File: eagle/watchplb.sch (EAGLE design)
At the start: 53 parts, among them IC1 SAM-M8Q, IC2 BM70BLES1FC2-0B03AA, Q1 8MHz / LFXTAL020423Reel, U1 MCP111-XXXXX/TO, U2 STM32L073RZ, U3 MCP2200-I/SS

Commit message: update
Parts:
- added C19: CSTCE12M0G15L99-R0, 12mhz osc:CSTCE8M00G52-R0
- added C20: 1uF, resistor:C-EUC0805
- added D1: S8NC-13, diode:DIODE-SMC
- added J1: (no value), SparkFun-Connectors:USB_MICRO-B_FEMALE-SMT
- added JP2: VIB_MOTOR, 619-28821, pinhead:PINHD-1X2
- added LED10: YELLOW, adafruit:LEDCHIP-LED0805
- added LED11, LED6, LED7, LED8: GREEN, adafruit:LEDCHIP-LED0805
- added LED12, LED9: RED, adafruit:LEDCHIP-LED0805
- added Q2: DMT5015LFDF, Hick:DMT5015LFDF
- added R18, R19, R20, R21, R22, R23, R24: 220R, resistor:R-EU_M0805
- added R25: 100k, resistor:R-EU_M0805
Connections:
- net N$10 renamed IND_LED_B
- net N$15 renamed IND_LED_W
- net N$17 renamed IND_LED_R
- net N$8 renamed IND_LED_G
- new net +5V: J1.VBUS, U3.VDD
- new net N$10: C19.33, U3.OSC2
- new net N$13: LED9.A, R21.2
- new net N$15: C19.11, U3.OSC1
- new net N$17: J1.D-, U3.D-
- new net N$19: LED6.A, R18.2
- new net N$20: J1.D+, U3.D+
- new net N$21: C20.1, U3.VUSB
- new net N$22: LED7.A, R19.2
- new net N$23: LED12.A, R24.2
- new net N$24: LED10.A, R22.2
- new net N$25: LED8.A, R20.2
- new net N$26: LED11.C, U3.GP6/RXLED
- new net N$27: LED12.C, U3.GP7/TXLED
- new net N$28: D1.A, JP2.2, Q2.D
- new net N$8: LED11.A, R23.2
- new net POW_LED_G1: R20.1, U2.PC4
- new net POW_LED_G2: R19.1, U2.PC5
- new net POW_LED_G3: R18.1, U2.PB0
- new net POW_LED_R: R21.1, U2.PA6
- new net POW_LED_Y: R22.1, U2.PA7
- new net SWD_RX: U3.RX
- new net SWD_RXD: U2.PA2
- new net SWD_TX: U3.TX
- new net SWD_TXD: U2.PA3
- new net V+: D1.C, JP2.1
- new net VIBRATOR: Q2.G, R25.1, U2.PA11
- net +3V3: now also R23.1, R24.1, U3.N_RST
- net GND: now also C19.22, C20.2, J1.GND, J1.SHIELD, LED10.C, LED6.C, LED7.C, LED8.C, LED9.C, Q2.S, R25.2, U3.VSS
- net GPS_RXD: now also U2.PC10; no longer U2.PA2
- net GPS_TXD: now also U2.PC11; no longer U2.PA3
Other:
- note added: "uart4 bzw lpuart1"
- note removed: "^^^^GPS UART2, crossed"
- moved on the sheet: C10, C11, C12, C13, C14, C15, C16, C17, C18, C4, C5, C6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

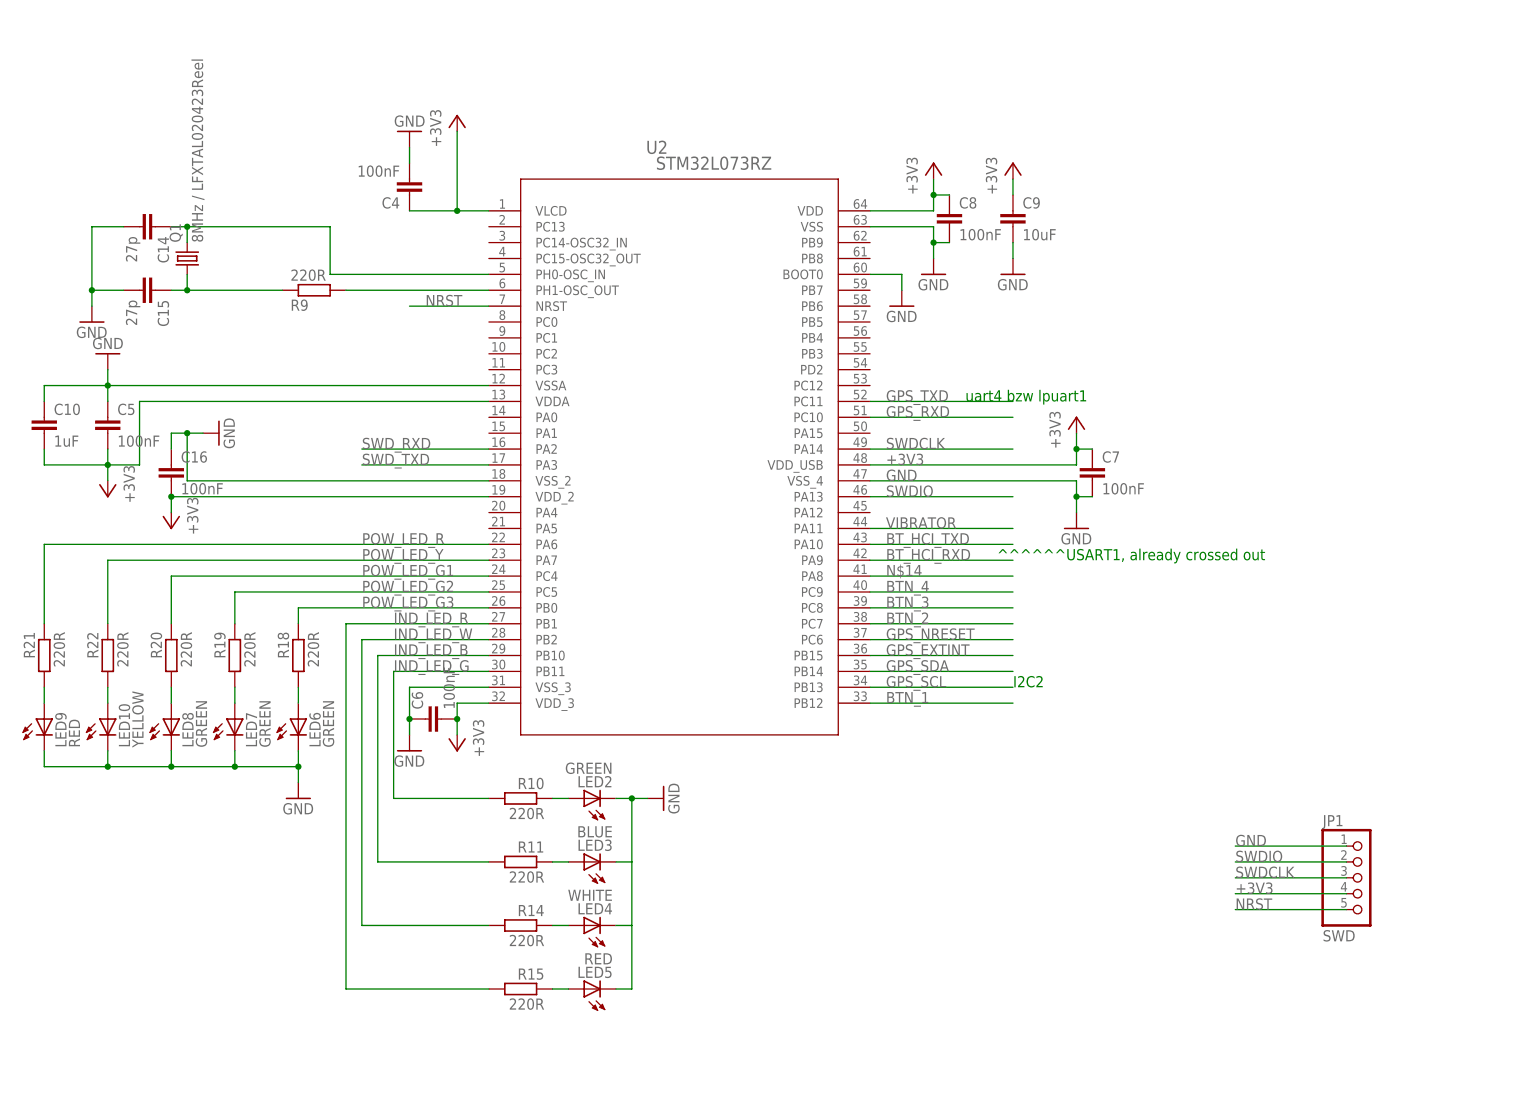
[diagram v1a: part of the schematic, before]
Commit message: added testpoints, moved pins so pb11 is free to make it pin kompatibel to another prozessor with more power
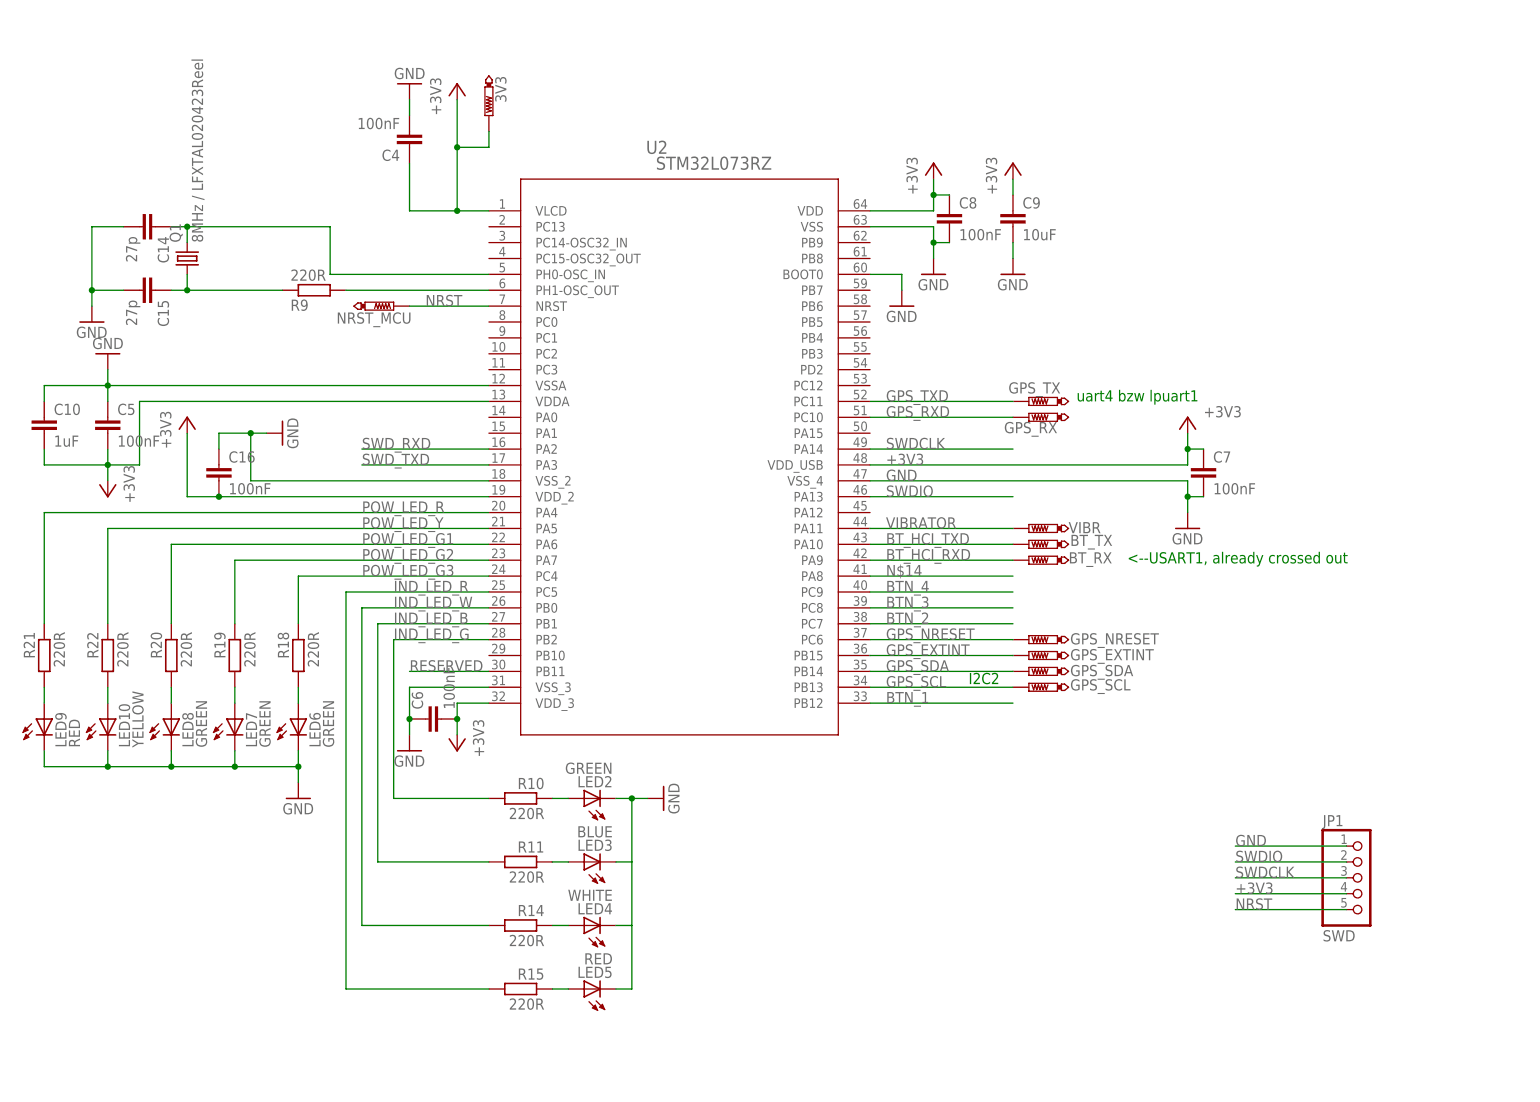
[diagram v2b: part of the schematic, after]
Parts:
- added 3V3, BT_RX, BT_TX, GPS_EXTINT, GPS_NRESET, GPS_RX, GPS_SCL, GPS_SDA, GPS_TX, NRST_MCU, VIBR: PTR1B2,54, testpad:PTR1B2,54
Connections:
- new net RESERVED: U2.PB11
- net +3V3: now also 3V3.TP
- net BT_HCI_RXD: now also BT_RX.TP
- net BT_HCI_TXD: now also BT_TX.TP
- net GPS_EXTINT: now also GPS_EXTINT.TP
- net GPS_NRESET: now also GPS_NRESET.TP
- net GPS_RXD: now also GPS_RX.TP
- net GPS_SCL: now also GPS_SCL.TP
- net GPS_SDA: now also GPS_SDA.TP
- net GPS_TXD: now also GPS_TX.TP
- net IND_LED_B: now also U2.PB1; no longer U2.PB10
- net IND_LED_G: now also U2.PB2; no longer U2.PB11
- net IND_LED_R: now also U2.PC5; no longer U2.PB1
- net IND_LED_W: now also U2.PB0; no longer U2.PB2
- net NRST: now also NRST_MCU.TP
- net POW_LED_G1: now also U2.PA6; no longer U2.PC4
- net POW_LED_G2: now also U2.PA7; no longer U2.PC5
- net POW_LED_G3: now also U2.PC4; no longer U2.PB0
- net POW_LED_R: now also U2.PA4; no longer U2.PA6
- net POW_LED_Y: now also U2.PA5; no longer U2.PA7
- net VIBRATOR: now also VIBR.TP
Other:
- note added: "<--USART1, already crossed out"
- note removed: "^^^^^^USART1, already crossed out"
- moved on the sheet: C16, C4, C7

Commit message: no message
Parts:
- added SWD_RXD, SWD_TXD, USB_5V, USB_D+, USB_D-: PTR1B2,54, testpad:PTR1B2,54
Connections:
- net +5V: now also USB_5V.TP
- net N$17: now also USB_D-.TP
- net N$20: now also USB_D+.TP
- net SWD_RXD: now also SWD_RXD.TP
- net SWD_TXD: now also SWD_TXD.TP
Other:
- moved on the sheet: C14, C15, C6, LED10, LED6, LED7, LED8, LED9, Q1, R18, R19, R20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

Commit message: added wakeup pin support and page for psu (empty atm)
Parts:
- added D2, D3, D4, D5: (no value), adafruit:DIODESOD-123
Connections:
- new net MCU_WAKEUP: D2.C, D3.C, D4.C, D5.C, U2.PA0
- net BTN_1: now also D2.A
- net BTN_2: now also D3.A
- net BTN_3: now also D4.A
- net BTN_4: now also D5.A
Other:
- note added: "Power Supply goes here"
- note added: "ein/ausschalter direkt nach batterie"
- moved on the sheet: D1, JP2, Q2, R25
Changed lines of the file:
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@@
 <part name="SWD_TXD" library="testpad" deviceset="PTR1" device="B2,54"/>
 <part name="SWD_RXD" library="testpad" deviceset="PTR1" device="B2,54"/>
+<part name="FRAME6" library="frames" deviceset="A4L-LOC" device=""/>
+<part name="D2" library="adafruit" deviceset="DIODE" device="SOD-123"/>
+<part name="D3" library="adafruit" deviceset="DIODE" device="SOD-123"/>
+<part name="D4" library="adafruit" deviceset="DIODE" device="SOD-123"/>
+<part name="D5" library="adafruit" deviceset="DIODE" device="SOD-123"/>
 </parts>
 <sheets>
@@
 <text x="185.928" y="262.128" size="1.778" layer="91">I2C2</text>
 <text x="203.2" y="307.34" size="1.778" layer="91">uart4 bzw lpuart1</text>
+<text x="561.34" y="365.76" size="1.778" layer="91">Power Supply goes here</text>
+<text x="561.34" y="360.68" size="1.778" layer="91">ein/ausschalter direkt nach batterie</text>
 </plain>
 <instances>
@@
 <instance part="+3V22" gate="G$1" x="431.8" y="309.88"/>
 <instance part="FRAME5" gate="G$1" x="553.72" y="0"/>
-<instance part="JP2" gate="G$1" x="642.62" y="78.74"/>
-<instance part="D1" gate="G$1" x="650.24" y="78.74" rot="R90"/>
-<instance part="P+2" gate="1" x="650.24" y="96.52"/>
-<instance part="Q2" gate="G$1" x="640.08" y="60.96"/>
-<instance part="GND25" gate="1" x="650.24" y="38.1"/>
-<instance part="R25" gate="G$1" x="632.46" y="50.8" rot="MR270"/>
+<instance part="JP2" gate="G$1" x="764.54" y="86.36"/>
+<instance part="D1" gate="G$1" x="772.16" y="86.36" rot="R90"/>
+<instance part="P+2" gate="1" x="772.16" y="104.14"/>
+<instance part="Q2" gate="G$1" x="762" y="68.58"/>
+<instance part="GND25" gate="1" x="772.16" y="45.72"/>
+<instance part="R25" gate="G$1" x="754.38" y="58.42" rot="MR270"/>
 <instance part="VIBR" gate="G$1" x="195.58" y="287.02" smashed="yes" rot="R90">
 <attribute name="NAME" x="201.93" y="286.258" size="1.778" layer="95"/>
@@
 <attribute name="TP_SIGNAL_NAME" x="83.82" y="298.45" size="1.778" layer="97" rot="R270"/>
 </instance>
+<instance part="FRAME6" gate="G$1" x="553.72" y="195.58"/>
+<instance part="D2" gate="G$1" x="601.98" y="99.06" rot="R180"/>
+<instance part="D3" gate="G$1" x="601.98" y="93.98" rot="R180"/>
+<instance part="D4" gate="G$1" x="601.98" y="88.9" rot="R180"/>
+<instance part="D5" gate="G$1" x="601.98" y="83.82" rot="R180"/>
 </instances>
 <busses>
@@
 <segment>
 <pinref part="Q2" gate="G$1" pin="S"/>
-<wire x1="645.16" y1="58.42" x2="650.24" y2="58.42" width="0.1524" layer="91"/>
-<wire x1="650.24" y1="58.42" x2="650.24" y2="43.18" width="0.1524" layer="91"/>
+<wire x1="767.08" y1="66.04" x2="772.16" y2="66.04" width="0.1524" layer="91"/>
+<wire x1="772.16" y1="66.04" x2="772.16" y2="50.8" width="0.1524" layer="91"/>
 <pinref part="GND25" gate="1" pin="GND"/>
 <pinref part="R25" gate="G$1" pin="2"/>
-<wire x1="650.24" y1="43.18" x2="650.24" y2="40.64" width="0.1524" layer="91"/>
-<wire x1="632.46" y1="45.72" x2="632.46" y2="43.18" width="0.1524" layer="91"/>
-<wire x1="632.46" y1="43.18" x2="650.24" y2="43.18" width="0.1524" layer="91"/>
-<junction x="650.24" y="43.18"/>
+<wire x1="772.16" y1="50.8" x2="772.16" y2="48.26" width="0.1524" layer="91"/>
+<wire x1="754.38" y1="53.34" x2="754.38" y2="50.8" width="0.1524" layer="91"/>
+<wire x1="754.38" y1="50.8" x2="772.16" y2="50.8" width="0.1524" layer="91"/>
+<junction x="772.16" y="50.8"/>
 </segment>
 </net>
@@
 <label x="172.72" y="271.78" size="1.778" layer="95"/>
 </segment>
+<segment>
+<pinref part="D3" gate="G$1" pin="A"/>
+<wire x1="604.52" y1="93.98" x2="619.76" y2="93.98" width="0.1524" layer="91"/>
+<label x="604.52" y="93.98" size="1.778" layer="95"/>
+</segment>
 </net>
 <net name="N$7" class="0">
@@
 <label x="172.72" y="259.08" size="1.778" layer="95"/>
 </segment>
+<segment>
+<pinref part="D2" gate="G$1" pin="A"/>
+<wire x1="604.52" y1="99.06" x2="619.76" y2="99.06" width="0.1524" layer="91"/>
+<label x="604.52" y="99.06" size="1.778" layer="95"/>
+</segment>
 </net>
 <net name="N$5" class="0">
@@
 <label x="172.72" y="274.32" size="1.778" layer="95"/>
 </segment>
+<segment>
+<pinref part="D4" gate="G$1" pin="A"/>
+<wire x1="604.52" y1="88.9" x2="619.76" y2="88.9" width="0.1524" layer="91"/>
+<label x="604.52" y="88.9" size="1.778" layer="95"/>
+</segment>
 </net>
 <net name="N$14" class="0">
@@
 <label x="172.72" y="276.86" size="1.778" layer="95"/>
 </segment>
+<segment>
+<pinref part="D5" gate="G$1" pin="A"/>
+<wire x1="604.52" y1="83.82" x2="619.76" y2="83.82" width="0.1524" layer="91"/>
+<label x="604.52" y="83.82" size="1.778" layer="95"/>
+</segment>
 </net>
 <net name="N$19" class="0">
@@
 <segment>
 <pinref part="JP2" gate="G$1" pin="2"/>
-<wire x1="640.08" y1="78.74" x2="640.08" y2="73.66" width="0.1524" layer="91"/>
+<wire x1="762" y1="86.36" x2="762" y2="81.28" width="0.1524" layer="91"/>
 <pinref part="D1" gate="G$1" pin="A"/>
-<wire x1="640.08" y1="73.66" x2="650.24" y2="73.66" width="0.1524" layer="91"/>
-<wire x1="650.24" y1="73.66" x2="650.24" y2="76.2" width="0.1524" layer="91"/>
+<wire x1="762" y1="81.28" x2="772.16" y2="81.28" width="0.1524" layer="91"/>
+<wire x1="772.16" y1="81.28" x2="772.16" y2="83.82" width="0.1524" layer="91"/>
 <pinref part="Q2" gate="G$1" pin="D"/>
-<wire x1="645.16" y1="63.5" x2="650.24" y2="63.5" width="0.1524" layer="91"/>
-<wire x1="650.24" y1="63.5" x2="650.24" y2="73.66" width="0.1524" layer="91"/>
-<junction x="650.24" y="73.66"/>
+<wire x1="767.08" y1="71.12" x2="772.16" y2="71.12" width="0.1524" layer="91"/>
+<wire x1="772.16" y1="71.12" x2="772.16" y2="81.28" width="0.1524" layer="91"/>
+<junction x="772.16" y="81.28"/>
 </segment>
 </net>
@@
 <segment>
 <pinref part="JP2" gate="G$1" pin="1"/>
-<wire x1="640.08" y1="81.28" x2="640.08" y2="86.36" width="0.1524" layer="91"/>
+<wire x1="762" y1="88.9" x2="762" y2="93.98" width="0.1524" layer="91"/>
 <pinref part="D1" gate="G$1" pin="C"/>
-<wire x1="640.08" y1="86.36" x2="650.24" y2="86.36" width="0.1524" layer="91"/>
-<wire x1="650.24" y1="86.36" x2="650.24" y2="81.28" width="0.1524" layer="91"/>
+<wire x1="762" y1="93.98" x2="772.16" y2="93.98" width="0.1524" layer="91"/>
+<wire x1="772.16" y1="93.98" x2="772.16" y2="88.9" width="0.1524" layer="91"/>
 <pinref part="P+2" gate="1" pin="V+"/>
-<wire x1="650.24" y1="86.36" x2="650.24" y2="93.98" width="0.1524" layer="91"/>
-<junction x="650.24" y="86.36"/>
+<wire x1="772.16" y1="93.98" x2="772.16" y2="101.6" width="0.1524" layer="91"/>
+<junction x="772.16" y="93.98"/>
 </segment>
 </net>
@@
 <pinref part="Q2" gate="G$1" pin="G"/>
 <pinref part="R25" gate="G$1" pin="1"/>
-<wire x1="635" y1="58.42" x2="632.46" y2="58.42" width="0.1524" layer="91"/>
-<wire x1="632.46" y1="58.42" x2="632.46" y2="55.88" width="0.1524" layer="91"/>
-<wire x1="632.46" y1="58.42" x2="617.22" y2="58.42" width="0.1524" layer="91"/>
-<junction x="632.46" y="58.42"/>
-<label x="617.22" y="58.42" size="1.778" layer="95"/>
+<wire x1="756.92" y1="66.04" x2="754.38" y2="66.04" width="0.1524" layer="91"/>
+<wire x1="754.38" y1="66.04" x2="754.38" y2="63.5" width="0.1524" layer="91"/>
+<wire x1="754.38" y1="66.04" x2="739.14" y2="66.04" width="0.1524" layer="91"/>
+<junction x="754.38" y="66.04"/>
+<label x="739.14" y="66.04" size="1.778" layer="95"/>
 </segment>
 <segment>
@@
 </segment>
 </net>
+<net name="MCU_WAKEUP" class="0">
+<segment>
+<pinref part="U2" gate="A" pin="PA0"/>
+<wire x1="109.22" y1="304.8" x2="88.9" y2="304.8" width="0.1524" layer="91"/>
+<label x="88.9" y="304.8" size="1.778" layer="95"/>
+</segment>
+<segment>
+<wire x1="576.58" y1="99.06" x2="596.9" y2="99.06" width="0.1524" layer="91"/>
+<label x="576.58" y="99.06" size="1.778" layer="95"/>
+<pinref part="D5" gate="G$1" pin="C"/>
+<wire x1="599.44" y1="83.82" x2="596.9" y2="83.82" width="0.1524" layer="91"/>
+<wire x1="596.9" y1="83.82" x2="596.9" y2="88.9" width="0.1524" layer="91"/>
+<junction x="596.9" y="99.06"/>
+<pinref part="D2" gate="G$1" pin="C"/>
+<wire x1="596.9" y1="88.9" x2="596.9" y2="93.98" width="0.1524" layer="91"/>
+<wire x1="596.9" y1="93.98" x2="596.9" y2="99.06" width="0.1524" layer="91"/>
+<wire x1="599.44" y1="99.06" x2="596.9" y2="99.06" width="0.1524" layer="91"/>
+<junction x="596.9" y="99.06"/>
+<pinref part="D3" gate="G$1" pin="C"/>
+<wire x1="599.44" y1="93.98" x2="596.9" y2="93.98" width="0.1524" layer="91"/>
+<junction x="596.9" y="93.98"/>
+<pinref part="D4" gate="G$1" pin="C"/>
+<wire x1="599.44" y1="88.9" x2="596.9" y2="88.9" width="0.1524" layer="91"/>
+<junction x="596.9" y="88.9"/>
+</segment>
+</net>
